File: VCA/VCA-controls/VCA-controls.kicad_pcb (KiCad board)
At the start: 2 copper layers, 30 x 114.5 mm, 19 parts, among them J1 AudioJack2, J10 Conn_01x03, J11 Conn_01x02, J12 Conn_01x03, J13 Conn_01x03, J14 Conn_01x03, J15 Conn_01x02, J2 AudioJack2, J3 AudioJack2, J4 AudioJack2, J5 AudioJack2, J6 AudioJack2, J7 AudioJack2, J8 AudioJack2, J9 Conn_01x03, SW1 SW_SPDT, SW2 SW_SPDT

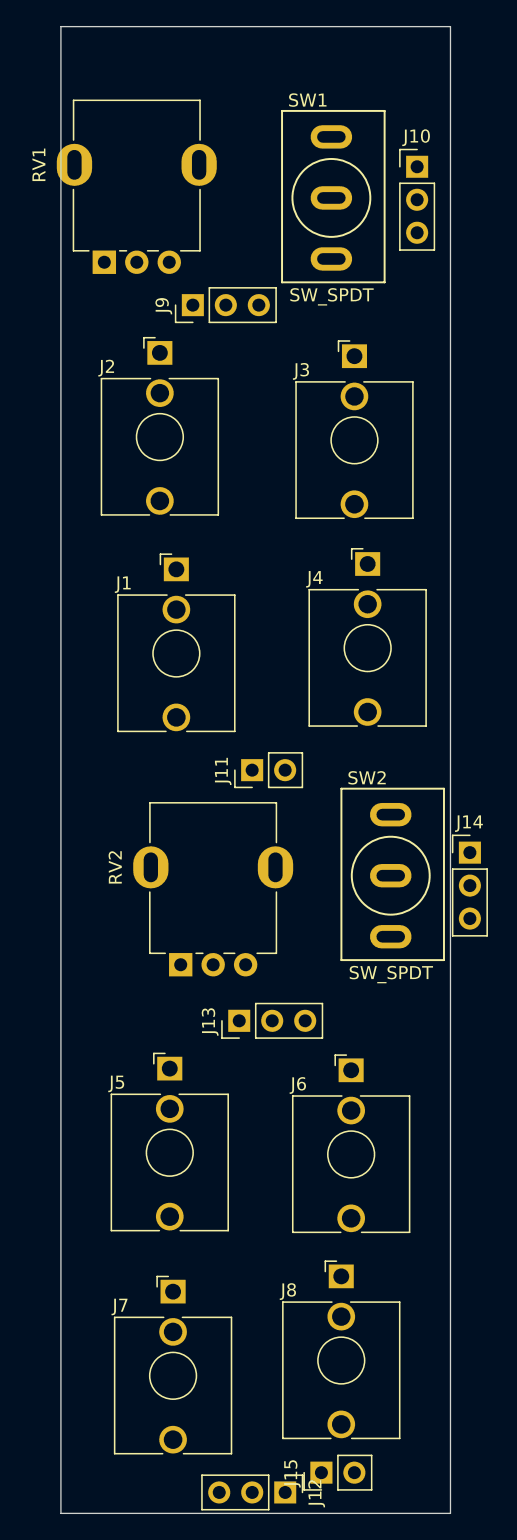
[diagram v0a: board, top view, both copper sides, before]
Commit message: VCA panel completed
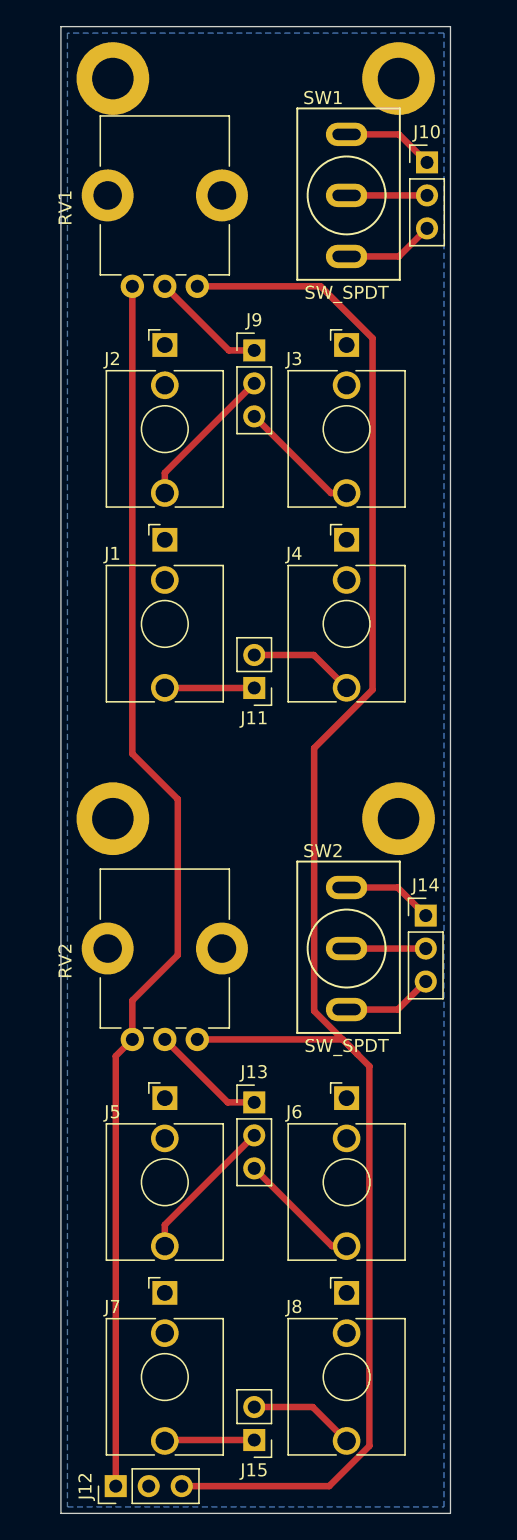
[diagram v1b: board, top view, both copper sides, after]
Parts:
- added H1: MountingHole_Pad, MountingHole:MountingHole_3.2mm_M3_DIN965_Pad, F.Cu at (4.00, 11.0)
- added H2: MountingHole_Pad, MountingHole:MountingHole_3.2mm_M3_DIN965_Pad, F.Cu at (26.0, 11.0)
- added H3: MountingHole_Pad, MountingHole:MountingHole_3.2mm_M3_DIN965_Pad, F.Cu at (26.0, 68.0)
- added H4: MountingHole_Pad, MountingHole:MountingHole_3.2mm_M3_DIN965_Pad, F.Cu at (4.00, 68.0)
- RV1, RV2: footprint benjiaomodular:Potentiometer_RV09 -> Library:Potentiometer_Bourns_PTV09A-1_Single_Vertical
- moved J12 13.1 mm to (4.22, 119.4), turned to 90 degrees
- moved RV1 6.94 mm to (8.00, 20.0), turned to 180 degrees
- moved SW2 6.56 mm to (22.0, 78.0)
- moved J13 6.39 mm to (14.9, 89.8), turned to 0 degrees
- moved J11 6.33 mm to (14.9, 57.9), turned to 180 degrees
- moved J14 5.92 mm to (28.1, 75.5)
- moved J9 5.88 mm to (14.9, 31.9), turned to 0 degrees
- moved J15 5.75 mm to (14.9, 115.9), turned to 180 degrees
- moved J4 2.47 mm to (22.0, 53.0)
- moved J1 2.45 mm to (8.00, 53.0)
- moved J5 2.31 mm to (8.00, 96.0)
- moved J6 2.17 mm to (22.0, 96.0)
- moved RV2 1.75 mm to (8.00, 78.0), turned to 180 degrees
- moved J8 1.34 mm to (22.0, 111.0)
- moved SW1 1.19 mm to (22.0, 20.0)
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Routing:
- net -12V: track 0.00 -> 132.6 mm
- net +12V: track 0.00 -> 95.8 mm
- net CV1B: track 0.00 -> 11.4 mm
- net CV1A: track 0.00 -> 11.3 mm
- net CV2B: track 0.00 -> 9.59 mm
- net CV2A: track 0.00 -> 9.56 mm
- net ADJA: track 0.00 -> 8.93 mm
- net ADJB: track 0.00 -> 8.90 mm
- net OUTB: track 0.00 -> 8.19 mm
- net OUTA: track 0.00 -> 8.16 mm
- net LOGA: track 0.00 -> 7.09 mm
- net LINA: track 0.00 -> 7.09 mm
- net LOGB: track 0.00 -> 6.99 mm
- net LINB: track 0.00 -> 6.99 mm
- net INB: track 0.00 -> 6.92 mm
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- added copper zone on B.Cu, net GND
